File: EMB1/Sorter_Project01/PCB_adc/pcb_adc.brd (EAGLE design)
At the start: 100 x 80 mm, 15 parts, among them K1 61201021621, Q1 IRF512, Q2 IRF512, Q3 IRF512

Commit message: updated PCB design
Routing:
- net N$10: track 5.08 -> 4.45 mm
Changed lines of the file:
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@@
 </signal>
 <signal name="N$10">
-<wire x1="34.925" y1="6.35" x2="34.925" y2="1.27" width="0.8128" layer="16"/>
+<wire x1="34.925" y1="1.27" x2="34.925" y2="5.715" width="0.4064" layer="16"/>
 </signal>
 </signals>

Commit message: report images added
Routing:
- net GND: track 229.7 -> 225.9 mm
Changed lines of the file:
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@@
 <contactref element="U$1" pad="14"/>
 <contactref element="SL1" pad="8"/>
-<contactref element="SL1" pad="10"/>
 <contactref element="K1" pad="2"/>
 <contactref element="K1" pad="4"/>
@@
 <wire x1="85.09" y1="27.94" x2="85.09" y2="30.48" width="0.8128" layer="16"/>
 <wire x1="59.6646" y1="8.9154" x2="59.69" y2="8.89" width="0.254" layer="16"/>
-<wire x1="57.15" y1="8.9154" x2="57.15" y2="8.89" width="0.254" layer="16"/>
 <wire x1="45.72" y1="68.58" x2="48.26" y2="68.58" width="0.8128" layer="16"/>
 <wire x1="48.26" y1="68.58" x2="50.8" y2="68.58" width="0.8128" layer="16"/>
 <wire x1="59.6646" y1="8.9154" x2="59.6392" y2="8.89" width="0.8128" layer="16"/>
-<wire x1="59.6392" y1="8.89" x2="57.15" y2="8.89" width="0.8128" layer="16"/>
 <wire x1="52.07" y1="8.89" x2="52.07" y2="12.7" width="0.8128" layer="16"/>
 <wire x1="52.07" y1="12.7" x2="57.15" y2="17.78" width="0.8128" layer="16"/>
@@
 <wire x1="53.34" y1="6.35" x2="55.88" y2="6.35" width="0.8128" layer="16"/>
 <wire x1="55.88" y1="6.35" x2="57.15" y2="7.62" width="0.8128" layer="16"/>
-<wire x1="57.15" y1="7.62" x2="57.15" y2="8.89" width="0.8128" layer="16"/>
 <wire x1="50.8" y1="68.58" x2="52.07" y2="67.31" width="0.4064" layer="16"/>
 <wire x1="52.07" y1="67.31" x2="54.61" y2="67.31" width="0.4064" layer="16"/>
@@
 <vertex x="38.1" y="30.48"/>
 </polygon>
-<wire x1="77.47" y1="30.48" x2="85.09" y2="30.48" width="0" layer="19" extent="1-1"/>
+<contactref element="SL1" pad="10"/>
+<wire x1="85.09" y1="30.48" x2="77.47" y2="30.48" width="0" layer="19" extent="1-1"/>
+<wire x1="57.15" y1="8.89" x2="59.6392" y2="8.89" width="0" layer="19" extent="16-16"/>
+<wire x1="57.15" y1="7.62" x2="57.15" y2="8.89" width="0" layer="19" extent="16-16"/>
 </signal>
 <signal name="+5V">

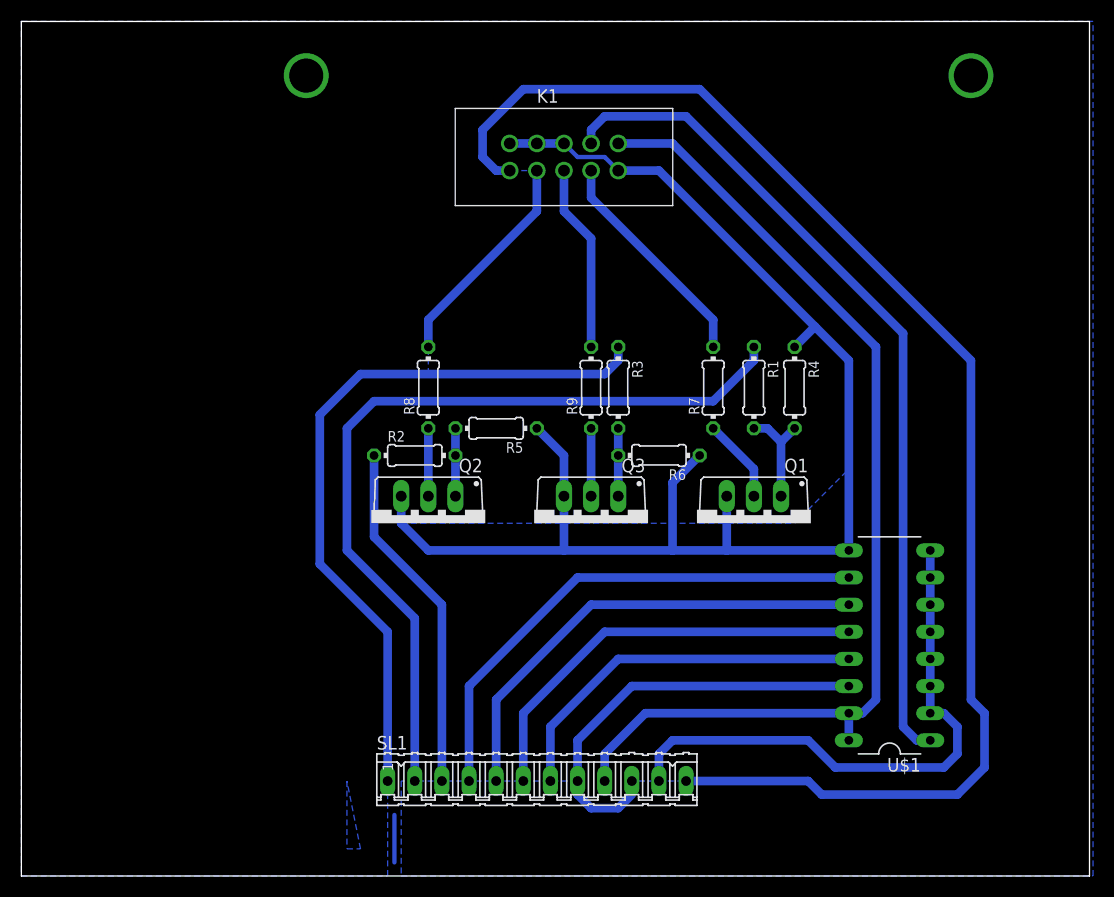
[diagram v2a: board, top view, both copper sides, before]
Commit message: VHDL updated, now the blinking works due to bug pulsing data-updated for too long
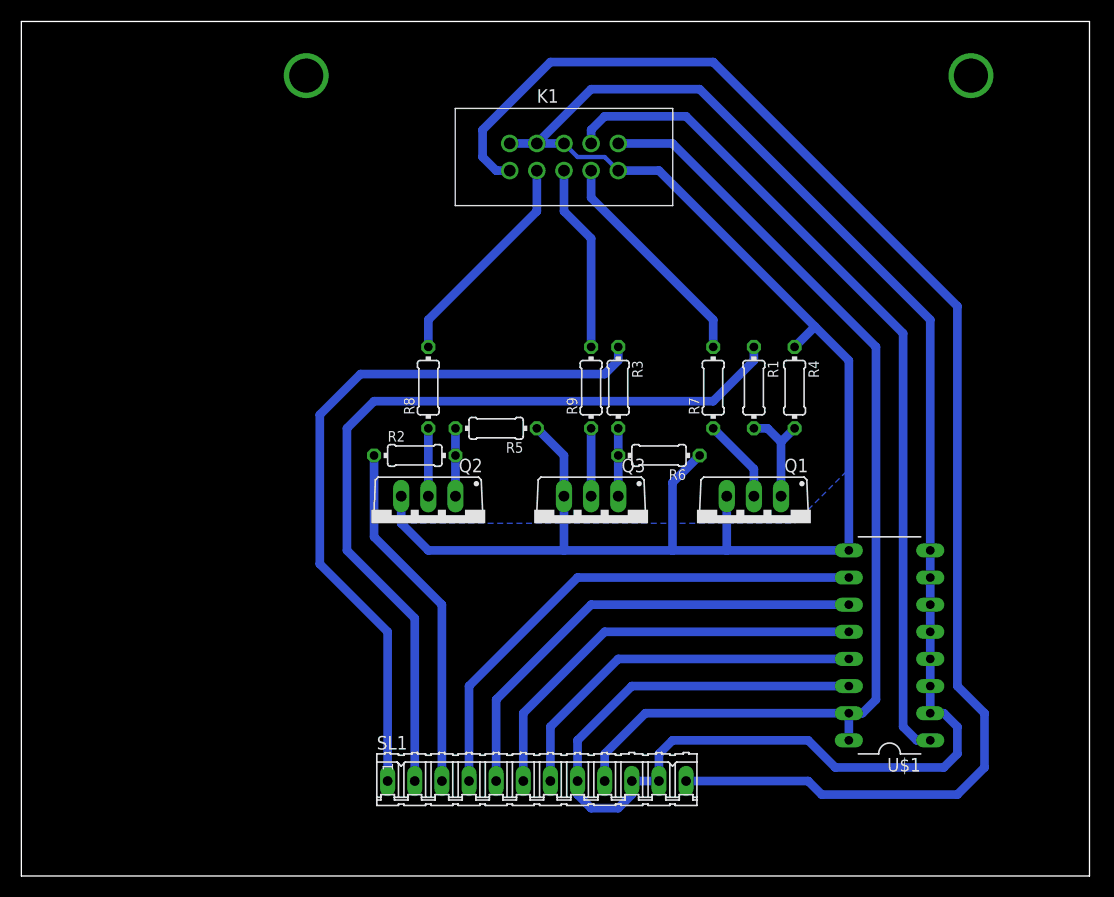
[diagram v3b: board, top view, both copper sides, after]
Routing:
- net GND: track 225.9 -> 299.1 mm
- net N$10: track 4.45 -> 0.00 mm
- net +12V: track 131.6 -> 135.9 mm
- removed copper zone on layer 16, net N$9
- removed copper zone on layer 16, net YTUYTUT
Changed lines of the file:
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@@
 </polygon>
 <contactref element="SL1" pad="10"/>
-<wire x1="85.09" y1="30.48" x2="77.47" y2="30.48" width="0" layer="19" extent="1-1"/>
-<wire x1="57.15" y1="8.89" x2="59.6392" y2="8.89" width="0" layer="19" extent="16-16"/>
-<wire x1="57.15" y1="7.62" x2="57.15" y2="8.89" width="0" layer="19" extent="16-16"/>
+<wire x1="85.09" y1="30.48" x2="85.09" y2="52.07" width="0.8128" layer="16"/>
+<wire x1="85.09" y1="52.07" x2="63.5" y2="73.66" width="0.8128" layer="16"/>
+<wire x1="63.5" y1="73.66" x2="53.34" y2="73.66" width="0.8128" layer="16"/>
+<wire x1="53.34" y1="73.66" x2="48.26" y2="68.58" width="0.8128" layer="16"/>
+<wire x1="59.6392" y1="8.89" x2="57.15" y2="8.89" width="0.8128" layer="16"/>
+<wire x1="57.15" y1="8.89" x2="57.15" y2="7.62" width="0.8128" layer="16"/>
 </signal>
 <signal name="+5V">
@@
 <wire x1="44.45" y1="66.04" x2="43.18" y2="67.31" width="0.8128" layer="16"/>
 <wire x1="43.18" y1="67.31" x2="43.18" y2="69.85" width="0.8128" layer="16"/>
-<wire x1="43.18" y1="69.85" x2="46.99" y2="73.66" width="0.8128" layer="16"/>
-<wire x1="46.99" y1="73.66" x2="63.5" y2="73.66" width="0.8128" layer="16"/>
-<wire x1="63.5" y1="73.66" x2="88.9" y2="48.26" width="0.8128" layer="16"/>
-<wire x1="88.9" y1="48.26" x2="88.9" y2="16.51" width="0.8128" layer="16"/>
-<wire x1="88.9" y1="16.51" x2="90.17" y2="15.24" width="0.8128" layer="16"/>
+<wire x1="87.63" y1="53.34" x2="87.63" y2="17.78" width="0.8128" layer="16"/>
+<wire x1="87.63" y1="17.78" x2="90.17" y2="15.24" width="0.8128" layer="16"/>
 <wire x1="90.17" y1="15.24" x2="90.17" y2="10.16" width="0.8128" layer="16"/>
 <wire x1="90.17" y1="10.16" x2="87.63" y2="7.62" width="0.8128" layer="16"/>
@@
 <wire x1="74.93" y1="7.62" x2="73.66" y2="8.89" width="0.8128" layer="16"/>
 <wire x1="73.66" y1="8.89" x2="62.23" y2="8.89" width="0.8128" layer="16"/>
+<wire x1="43.18" y1="69.85" x2="49.53" y2="76.2" width="0.8128" layer="16"/>
+<wire x1="49.53" y1="76.2" x2="64.77" y2="76.2" width="0.8128" layer="16"/>
+<wire x1="64.77" y1="76.2" x2="87.63" y2="53.34" width="0.8128" layer="16"/>
 </signal>
 <signal name="N$6">
@@
 <via x="88.9" y="74.93" extent="1-16" drill="3.2"/>
 </signal>
-<signal name="N$9">
-<polygon width="0.8128" layer="16" isolate="12.7" thermals="no">
-<vertex x="30.48" y="8.89"/>
-<vertex x="30.48" y="2.54"/>
-<vertex x="31.75" y="2.54"/>
-</polygon>
-</signal>
-<signal name="YTUYTUT">
-<polygon width="0.8128" layer="16" isolate="1.27" thermals="no">
-<vertex x="34.29" y="0"/>
-<vertex x="34.29" y="22.86"/>
-<vertex x="27.94" y="29.21"/>
-<vertex x="27.94" y="43.18"/>
-<vertex x="31.75" y="46.99"/>
-<vertex x="38.1" y="46.99"/>
-<vertex x="38.1" y="52.07"/>
-<vertex x="48.26" y="62.23"/>
-<vertex x="48.26" y="66.04"/>
-<vertex x="44.45" y="66.04"/>
-<vertex x="43.18" y="67.31"/>
-<vertex x="43.18" y="69.85"/>
-<vertex x="46.99" y="73.66"/>
-<vertex x="63.5" y="73.66"/>
-<vertex x="88.9" y="48.26"/>
-<vertex x="88.9" y="16.51"/>
-<vertex x="90.17" y="15.24"/>
-<vertex x="90.17" y="10.16"/>
-<vertex x="87.63" y="7.62"/>
-<vertex x="74.93" y="7.62"/>
-<vertex x="73.66" y="8.89"/>
-<vertex x="57.15" y="8.89"/>
-<vertex x="57.15" y="7.62"/>
-<vertex x="55.88" y="6.35"/>
-<vertex x="53.34" y="6.35"/>
-<vertex x="52.07" y="7.62"/>
-<vertex x="52.07" y="8.89"/>
-<vertex x="35.56" y="8.89"/>
-<vertex x="35.56" y="0"/>
-<vertex x="100.33" y="0"/>
-<vertex x="100.33" y="80.01"/>
-<vertex x="0" y="80.01"/>
-<vertex x="0" y="0"/>
-</polygon>
-</signal>
-<signal name="N$10">
-<wire x1="34.925" y1="1.27" x2="34.925" y2="5.715" width="0.4064" layer="16"/>
-</signal>
 </signals>

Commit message: report updated
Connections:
- new net +3V3: SL1.9, U$1.15, U$1.16
- net +5V: no longer SL1.9, U$1.15, U$1.16
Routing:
- net +5V: track 97.6 -> 66.8 mm
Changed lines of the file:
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@@
 </signal>
 <signal name="+5V">
-<contactref element="U$1" pad="15"/>
-<contactref element="U$1" pad="16"/>
-<contactref element="SL1" pad="9"/>
 <contactref element="K1" pad="10"/>
-<wire x1="77.47" y1="12.7" x2="77.47" y2="15.24" width="0.8128" layer="16"/>
-<wire x1="77.47" y1="15.24" x2="58.42" y2="15.24" width="0.8128" layer="16"/>
-<wire x1="58.42" y1="15.24" x2="54.61" y2="11.43" width="0.8128" layer="16"/>
-<wire x1="54.61" y1="11.43" x2="54.61" y2="8.89" width="0.8128" layer="16"/>
 <wire x1="55.88" y1="68.58" x2="60.96" y2="68.58" width="0.8128" layer="16"/>
 <wire x1="60.96" y1="68.58" x2="80.01" y2="49.53" width="0.8128" layer="16"/>
 <wire x1="80.01" y1="49.53" x2="80.01" y2="16.51" width="0.8128" layer="16"/>
 <wire x1="80.01" y1="16.51" x2="78.74" y2="15.24" width="0.8128" layer="16"/>
-<wire x1="78.74" y1="15.24" x2="77.47" y2="15.24" width="0.8128" layer="16"/>
 </signal>
 <signal name="C_RED">
@@
 <via x="88.9" y="74.93" extent="1-16" drill="3.2"/>
 </signal>
+<signal name="+3V3">
+<contactref element="U$1" pad="15"/>
+<contactref element="U$1" pad="16"/>
+<contactref element="SL1" pad="9"/>
+<wire x1="77.47" y1="12.7" x2="77.47" y2="15.24" width="0" layer="19" extent="1-1"/>
+<wire x1="54.61" y1="8.89" x2="77.47" y2="12.7" width="0" layer="19" extent="1-1"/>
+</signal>
 </signals>
